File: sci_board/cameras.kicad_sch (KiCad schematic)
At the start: 0 parts

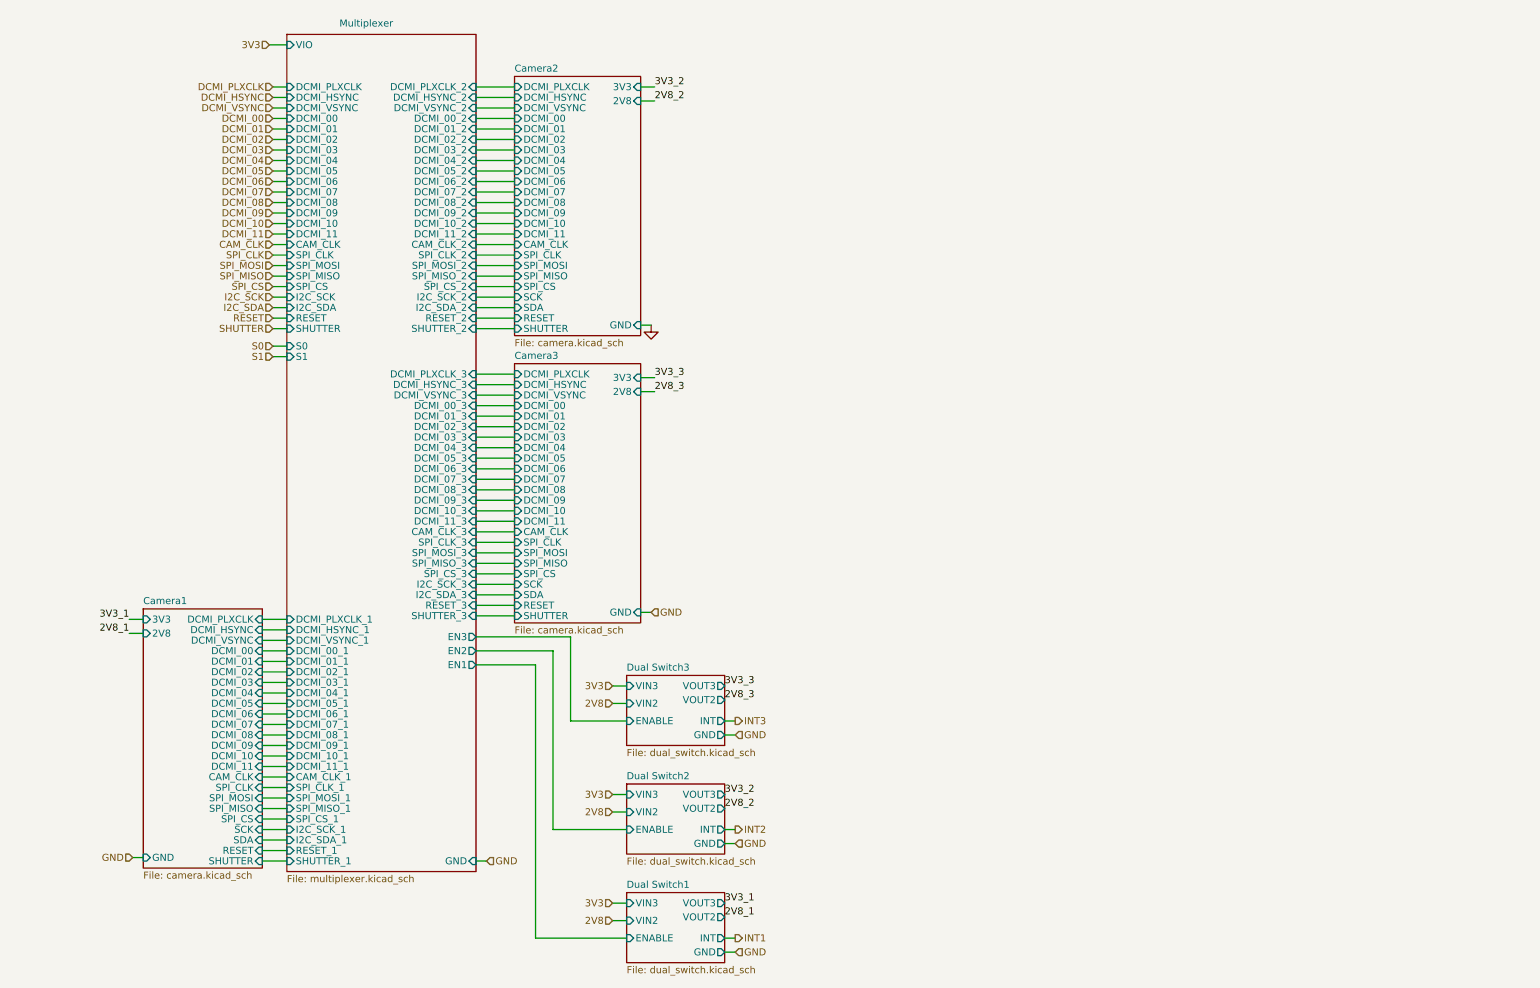
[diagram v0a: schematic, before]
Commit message: cameras have fcp connectors, use data 2:9, and need a clock
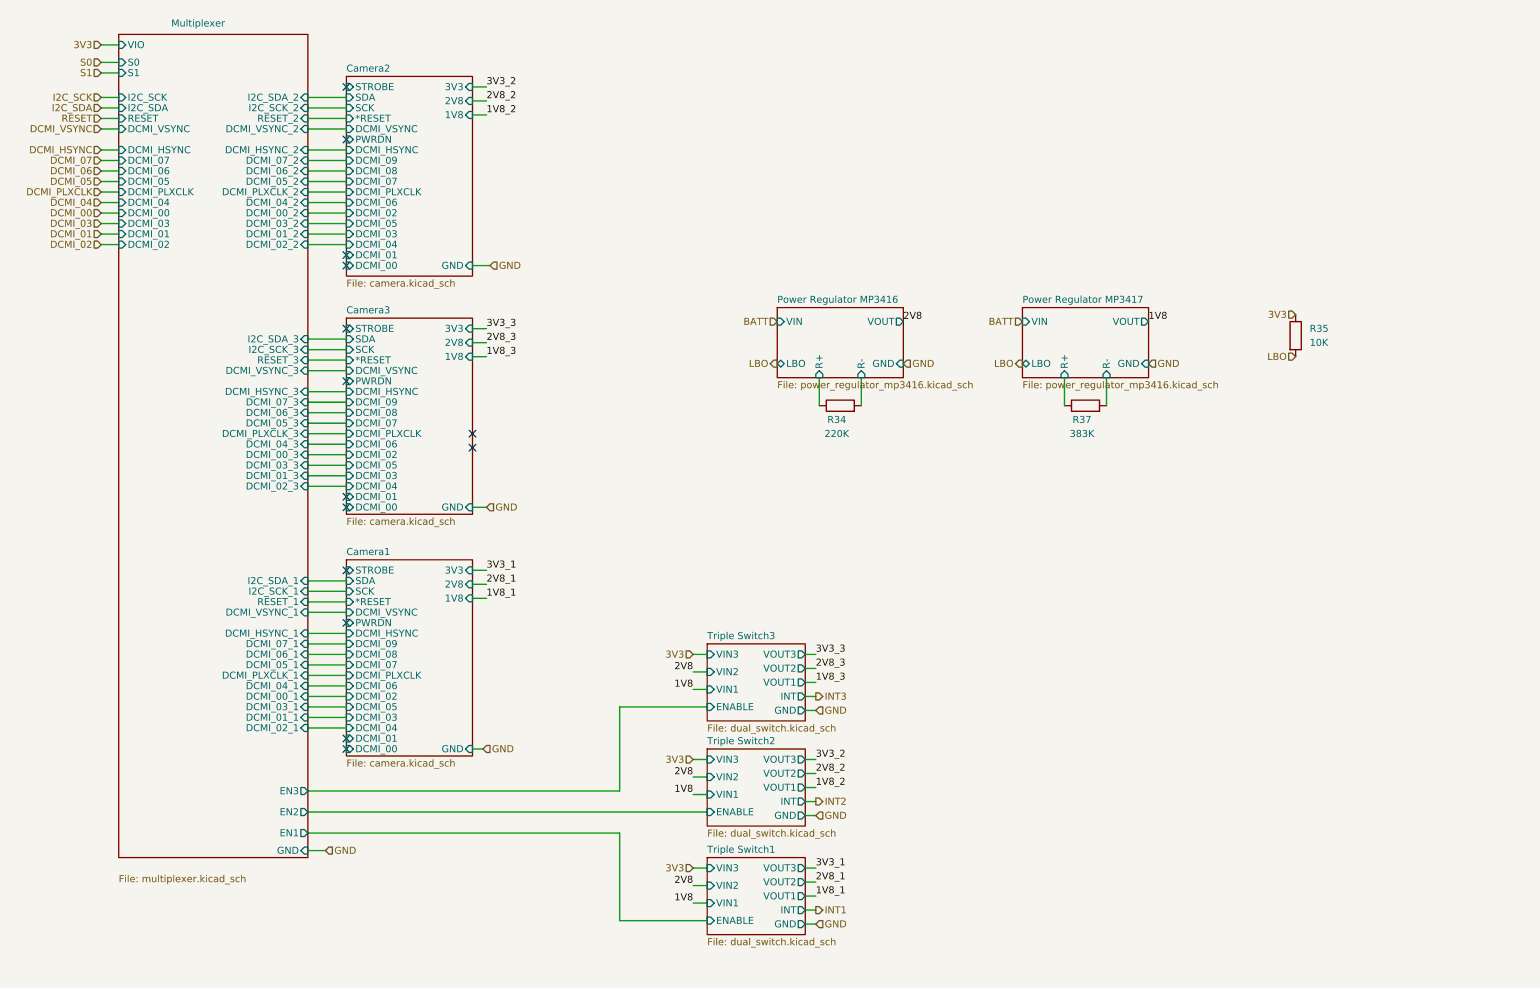
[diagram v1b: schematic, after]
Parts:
- added R34: 220K, symbol Device:R
- added R35: 10K, symbol Device:R
- added R37: 383K, symbol Device:R
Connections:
- net 3V3: now also R35.1
- new net LBO: R35.2
- new net Power Regulator MP3416/R+: R34.1
- new net Power Regulator MP3416/R-: R34.2
- new net Power Regulator MP3417/R+: R37.1
- new net Power Regulator MP3417/R-: R37.2
- no-connect marks 0 -> 14
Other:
- sheet Dual Switch3 renamed Triple Switch3
- removed sheet Dual Switch1
- removed sheet Dual Switch2
- added sheet Power Regulator MP3416 (power_regulator_mp3416.kicad_sch)
- added sheet Power Regulator MP3417 (power_regulator_mp3416.kicad_sch)
- added sheet Triple Switch1 (dual_switch.kicad_sch)
- added sheet Triple Switch2 (dual_switch.kicad_sch)
- sheet Camera1 ports: added *RESET, 1V8, PWRDN, STROBE; removed CAM_CLK, DCMI_10, DCMI_11, RESET, SHUTTER, SPI_CLK, SPI_CS, SPI_MISO, SPI_MOSI
- sheet Camera2 ports: added *RESET, 1V8, PWRDN, STROBE; removed CAM_CLK, DCMI_10, DCMI_11, RESET, SHUTTER, SPI_CLK, SPI_CS, SPI_MISO, SPI_MOSI
- sheet Camera3 ports: added *RESET, 1V8, PWRDN, STROBE; removed CAM_CLK, DCMI_10, DCMI_11, RESET, SHUTTER, SPI_CLK, SPI_CS, SPI_MISO, SPI_MOSI
- sheet Multiplexer ports: added none; removed CAM_CLK, CAM_CLK_1, CAM_CLK_2, CAM_CLK_3, DCMI_08, DCMI_08_1, DCMI_08_2, DCMI_08_3, DCMI_09, DCMI_09_1, DCMI_09_2, DCMI_09_3, DCMI_10, DCMI_10_1, DCMI_10_2, DCMI_10_3, DCMI_11, DCMI_11_1, DCMI_11_2, DCMI_11_3, SHUTTER, SHUTTER_1, SHUTTER_2, SHUTTER_3, SPI_CLK, SPI_CLK_1, SPI_CLK_2, SPI_CLK_3, SPI_CS, SPI_CS_1, SPI_CS_2, SPI_CS_3, SPI_MISO, SPI_MISO_1, SPI_MISO_2, SPI_MISO_3, SPI_MOSI, SPI_MOSI_1, SPI_MOSI_2, SPI_MOSI_3
- sheet Triple Switch3 ports: added VIN1, VOUT1; removed none

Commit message: begin to update the pcb
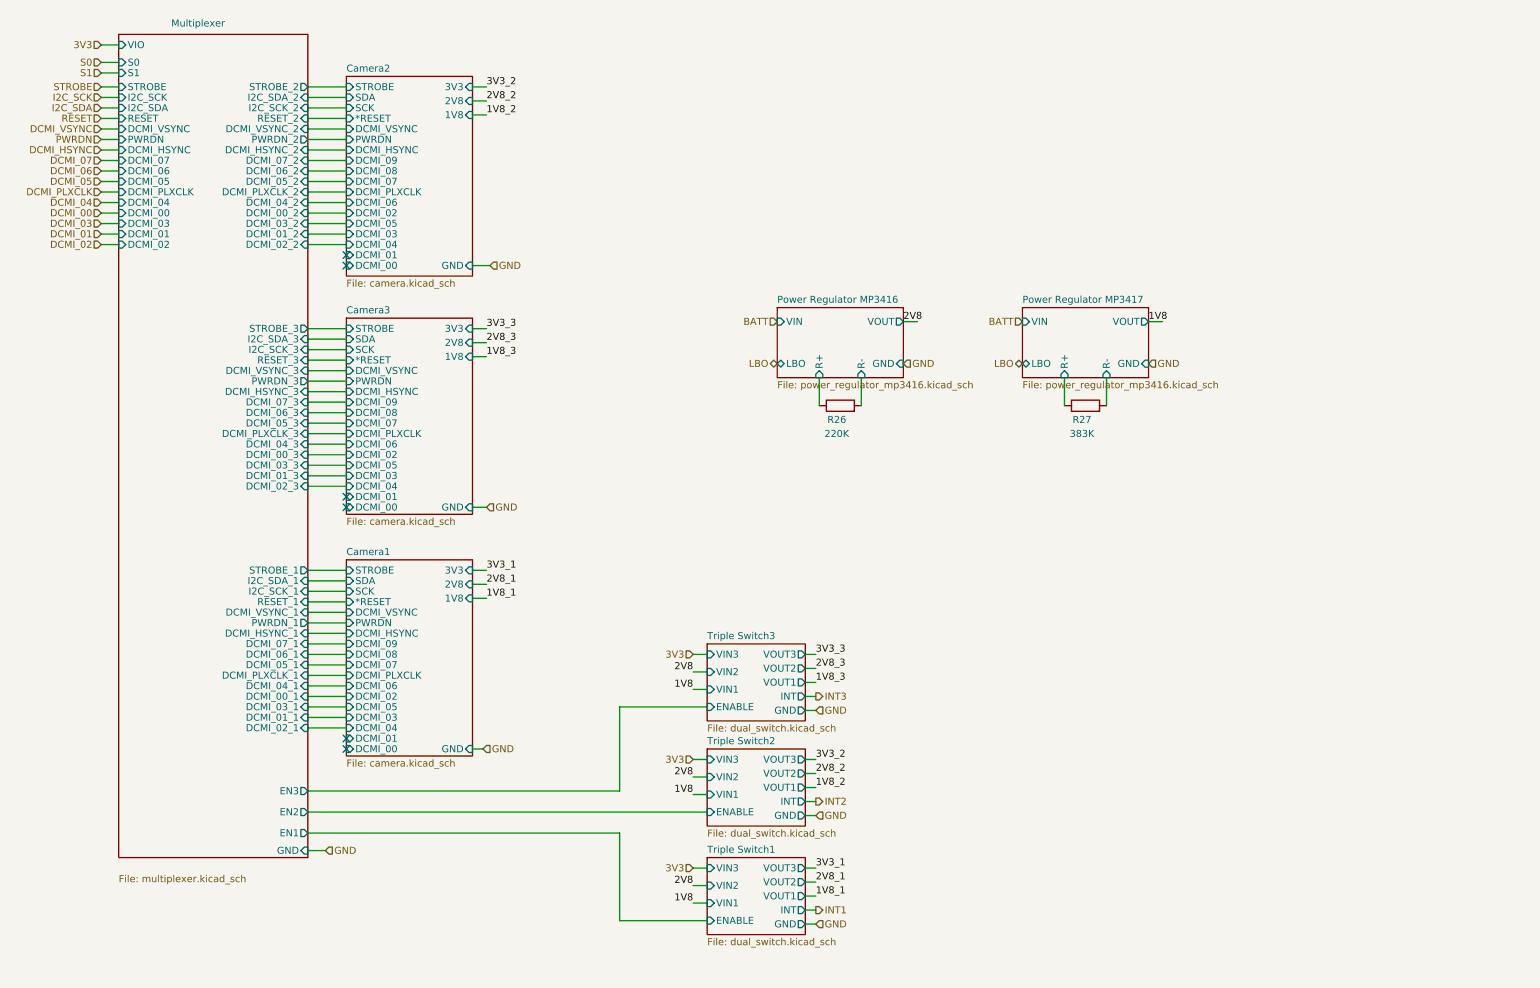
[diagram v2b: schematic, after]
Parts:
- removed R35: 10K, symbol Device:R
- R26: renamed from R34; footprint (none) -> Resistor_SMD:R_0603_1608Metric_Pad0.98x0.95mm_HandSolder
- R27: renamed from R37; footprint (none) -> Resistor_SMD:R_0603_1608Metric_Pad0.98x0.95mm_HandSolder
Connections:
- no-connect marks 14 -> 6
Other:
- sheet Multiplexer ports: added PWRDN, PWRDN_1, PWRDN_2, PWRDN_3, STROBE, STROBE_1, STROBE_2, STROBE_3; removed none
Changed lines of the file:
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@@
 	(paper "A4")
 	(no_connect
-		(at 73.66 120.65)
-	)
-	(no_connect
-		(at 73.66 86.36)
-	)
-	(no_connect
-		(at 96.52 95.885)
-	)
-	(no_connect
-		(at 73.66 33.02)
-	)
-	(no_connect
-		(at 73.66 76.835)
-	)
-	(no_connect
 		(at 73.66 107.315)
 	)
@@
 	)
 	(no_connect
-		(at 96.52 98.425)
-	)
-	(no_connect
 		(at 73.66 109.22)
 	)
 	(no_connect
-		(at 73.66 130.175)
-	)
-	(no_connect
-		(at 73.66 42.545)
-	)
-	(no_connect
 		(at 73.66 65.405)
 	)
@@
 	(wire
 		(pts
+			(xy 177.165 75.565) (xy 174.625 75.565)
+		)
+		(stroke
+			(width 0)
+			(type default)
+		)
+	)
+	(wire
+		(pts
 			(xy 66.675 122.555) (xy 73.66 122.555)
 		)
@@
 	(wire
 		(pts
+			(xy 66.675 120.65) (xy 73.66 120.65)
+		)
+		(stroke
+			(width 0)
+			(type default)
+		)
+	)
+	(wire
+		(pts
 			(xy 66.675 141.605) (xy 73.66 141.605)
 		)
@@
 	(wire
 		(pts
+			(xy 29.21 33.02) (xy 32.385 33.02)
+		)
+		(stroke
+			(width 0)
+			(type default)
+		)
+	)
+	(wire
+		(pts
 			(xy 66.675 93.98) (xy 73.66 93.98)
 		)
@@
 	(wire
 		(pts
+			(xy 66.675 76.835) (xy 73.66 76.835)
+		)
+		(stroke
+			(width 0)
+			(type default)
+		)
+	)
+	(wire
+		(pts
 			(xy 66.675 95.885) (xy 73.66 95.885)
 		)
@@
 	(wire
 		(pts
+			(xy 221.615 75.565) (xy 219.075 75.565)
+		)
+		(stroke
+			(width 0)
+			(type default)
+		)
+	)
+	(wire
+		(pts
+			(xy 66.675 33.02) (xy 73.66 33.02)
+		)
+		(stroke
+			(width 0)
+			(type default)
+		)
+	)
+	(wire
+		(pts
 			(xy 99.06 35.56) (xy 96.52 35.56)
 		)
@@
 	(wire
 		(pts
+			(xy 29.21 42.545) (xy 32.385 42.545)
+		)
+		(stroke
+			(width 0)
+			(type default)
+		)
+	)
+	(wire
+		(pts
 			(xy 136.525 139.065) (xy 139.065 139.065)
 		)
@@
 	(wire
 		(pts
+			(xy 66.675 42.545) (xy 73.66 42.545)
+		)
+		(stroke
+			(width 0)
+			(type default)
+		)
+	)
+	(wire
+		(pts
 			(xy 29.21 38.735) (xy 32.385 38.735)
 		)
@@
 	(wire
 		(pts
+			(xy 66.675 130.175) (xy 73.66 130.175)
+		)
+		(stroke
+			(width 0)
+			(type default)
+		)
+	)
+	(wire
+		(pts
 			(xy 66.675 143.51) (xy 73.66 143.51)
 		)
@@
 	(wire
 		(pts
+			(xy 66.675 86.36) (xy 73.66 86.36)
+		)
+		(stroke
+			(width 0)
+			(type default)
+		)
+	)
+	(wire
+		(pts
 			(xy 99.06 79.375) (xy 96.52 79.375)
 		)
@@
 	)
 	(hierarchical_label "LBO"
-		(shape output)
+		(shape tri_state)
 		(at 196.215 83.185 180)
 		(fields_autoplaced yes)
@@
 		)
 	)
+	(hierarchical_label "STROBE"
+		(shape input)
+		(at 29.21 33.02 180)
+		(fields_autoplaced yes)
+		(effects
+			(font
+				(size 1.27 1.27)
+			)
+			(justify right)
+		)
+	)
 	(hierarchical_label "GND"
 		(shape input)
@@
 	)
 	(hierarchical_label "LBO"
-		(shape output)
+		(shape tri_state)
 		(at 151.765 83.185 180)
 		(fields_autoplaced yes)
@@
 		)
 	)
-	(hierarchical_label "3V3"
-		(shape input)
-		(at 245.745 74.295 180)
-		(fields_autoplaced yes)
-		(effects
-			(font
-				(size 1.27 1.27)
-			)
-			(justify right)
-		)
-	)
 	(hierarchical_label "GND"
 		(shape input)
@@
 		)
 	)
-	(hierarchical_label "DCMI_07"
+	(hierarchical_label "PWRDN"
 		(shape input)
-		(at 29.21 46.355 180)
+		(at 29.21 42.545 180)
 		(fields_autoplaced yes)
 		(effects
@@
 		)
 	)
-	(hierarchical_label "LBO"
+	(hierarchical_label "DCMI_07"
 		(shape input)
-		(at 245.745 81.915 180)
+		(at 29.21 46.355 180)
 		(fields_autoplaced yes)
 		(effects
@@
 	(symbol
 		(lib_id "Device:R")
-		(at 245.745 78.105 0)
-		(unit 1)
-		(exclude_from_sim no)
-		(in_bom yes)
-		(on_board yes)
-		(dnp no)
-		(fields_autoplaced yes)
-		(property "Reference" "R35"
-			(at 248.285 76.8349 0)
-			(effects
-				(font
-					(size 1.27 1.27)
-				)
-				(justify left)
-			)
-		)
-		(property "Value" "10K"
-			(at 248.285 79.3749 0)
-			(effects
-				(font
-					(size 1.27 1.27)
-				)
-				(justify left)
-			)
-		)
-		(property "Footprint" ""
-			(at 243.967 78.105 90)
-			(effects
-				(font
-					(size 1.27 1.27)
-				)
-				(hide yes)
-			)
-		)
-		(property "Datasheet" "~"
-			(at 245.745 78.105 0)
-			(effects
-				(font
-					(size 1.27 1.27)
-				)
-				(hide yes)
-			)
-		)
-		(property "Description" "Resistor"
-			(at 245.745 78.105 0)
-			(effects
-				(font
-					(size 1.27 1.27)
-				)
-				(hide yes)
-			)
-		)
-		(pin "1"
-		)
-		(pin "2"
-		)
-		(instances
-			(project "sci_board"
-				(path "/b4b2c88d-f6cd-4e60-862d-e21f68728580/5e5b27f8-7a4c-45d0-95f8-aff71797fcd3"
-					(reference "R35")
-					(unit 1)
-				)
-			)
-		)
-	)
-	(symbol
-		(lib_id "Device:R")
 		(at 163.195 90.805 90)
 		(unit 1)
@@
 		(on_board yes)
 		(dnp no)
-		(property "Reference" "R34"
+		(property "Reference" "R26"
 			(at 162.56 93.345 90)
 			(effects
@@
 			)
 		)
-		(property "Footprint" ""
+		(property "Footprint" "Resistor_SMD:R_0603_1608Metric_Pad0.98x0.95mm_HandSolder"
 			(at 163.195 92.583 90)
 			(effects
@@
 			(project "sci_board"
 				(path "/b4b2c88d-f6cd-4e60-862d-e21f68728580/5e5b27f8-7a4c-45d0-95f8-aff71797fcd3"
-					(reference "R34")
+					(reference "R26")
 					(unit 1)
 				)
@@
 		(on_board yes)
 		(dnp no)
-		(property "Reference" "R37"
+		(property "Reference" "R27"
 			(at 207.01 93.345 90)
 			(effects
@@
 			)
 		)
-		(property "Footprint" ""
+		(property "Footprint" "Resistor_SMD:R_0603_1608Metric_Pad0.98x0.95mm_HandSolder"
 			(at 207.645 92.583 90)
 			(effects
@@
 			(project "sci_board"
 				(path "/b4b2c88d-f6cd-4e60-862d-e21f68728580/5e5b27f8-7a4c-45d0-95f8-aff71797fcd3"
-					(reference "R37")
+					(reference "R27")
 					(unit 1)
 				)
@@
 			(effects
 				(font
+					(size 1.27 1.27)
+				)
+				(justify right)
+			)
+		)
+		(pin "STROBE_2" output
+			(at 66.675 33.02 0)
+			(effects
+				(font
+					(size 1.27 1.27)
+				)
+				(justify right)
+			)
+		)
+		(pin "STROBE_3" output
+			(at 66.675 76.835 0)
+			(effects
+				(font
+					(size 1.27 1.27)
+				)
+				(justify right)
+			)
+		)
+		(pin "STROBE_1" output
+			(at 66.675 120.65 0)
+			(effects
+				(font
+					(size 1.27 1.27)
+				)
+				(justify right)
+			)
+		)
+		(pin "STROBE" input
+			(at 32.385 33.02 180)
+			(effects
+				(font
+					(size 1.27 1.27)
+				)
+				(justify left)
+			)
+		)
+		(pin "PWRDN_2" output
+			(at 66.675 42.545 0)
+			(effects
+				(font
+					(size 1.27 1.27)
+				)
+				(justify right)
+			)
+		)
+		(pin "PWRDN_1" output
+			(at 66.675 130.175 0)
+			(effects
+				(font
+					(size 1.27 1.27)
+				)
+				(justify right)
+			)
+		)
+		(pin "PWRDN" input
+			(at 32.385 42.545 180)
+			(effects
+				(font
+					(size 1.27 1.27)
+				)
+				(justify left)
+			)
+		)
+		(pin "PWRDN_3" output
+			(at 66.675 86.36 0)
+			(effects
+				(font

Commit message: continue layout
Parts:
- added C51: 100n, Capacitor_SMD:C_0402_1005Metric_Pad0.74x0.62mm_HandSolder, symbol Device:C
- added X1: TG2520SMN 24.0000M-MCGNNM0, Project:TG-3541CE_EPS, symbol Project:TG-3541CE-1K
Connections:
- net 3V3: now also C51.1, X1.1 (OE), X1.2 (Vcc), X1.3 (Vcc)
- net GND: now also C51.2, X1.5 (GND), X1.7 (GND), X1.8 (GND), X1.9 (GND)
- new net XCLK: X1.4 (OUT)
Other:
- sheet Camera1 ports: added XCLK; removed none
- sheet Camera2 ports: added XCLK; removed none
- sheet Camera3 ports: added XCLK; removed none
- sheet Multiplexer ports: added XCLK, XCLK_1, XCLK_2, XCLK_3; removed none
- moved on the sheet: R26, R27
